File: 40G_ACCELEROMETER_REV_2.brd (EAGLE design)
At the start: 25.5 x 26.9 mm, 25 parts, among them IC1 3.3V_LDO, IC2 X_BUFFER, IC3 Y_BUFFER, IC4 Z_BUFFER

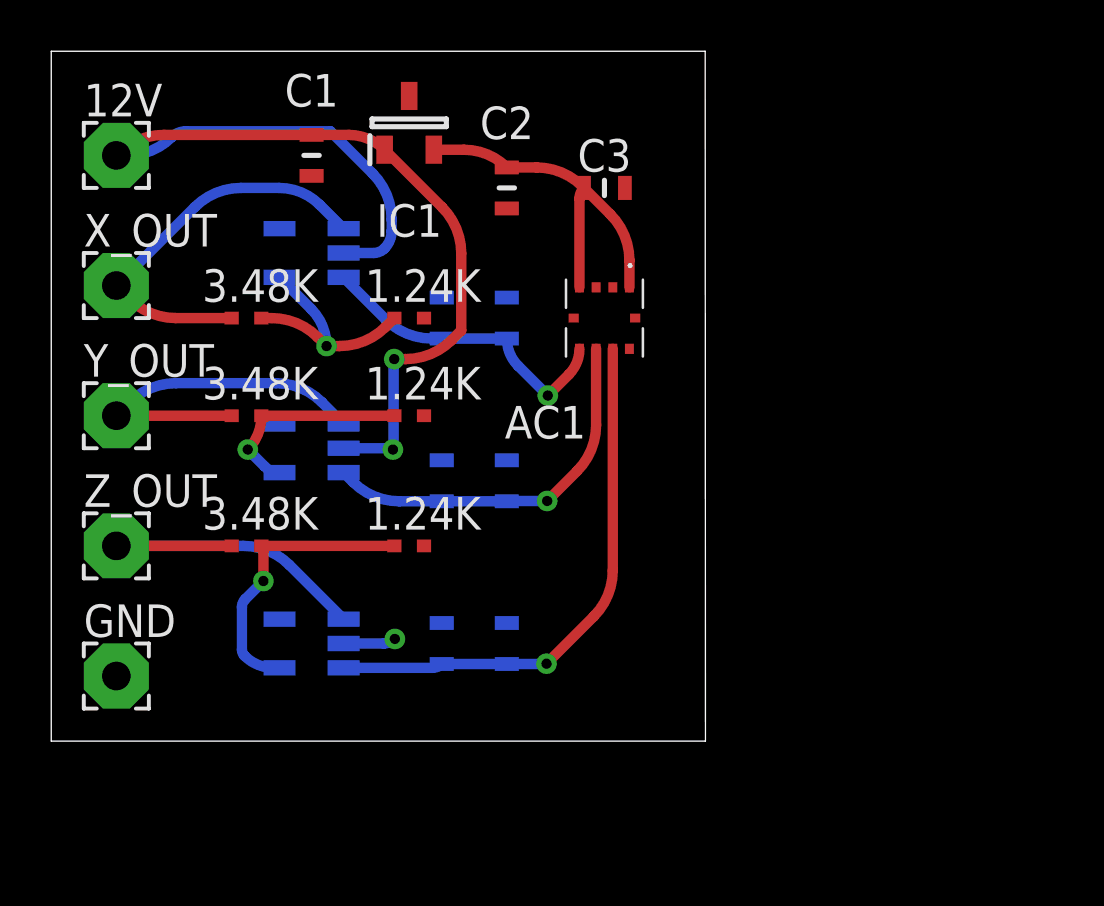
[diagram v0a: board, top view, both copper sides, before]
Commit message: Added ground plane to board
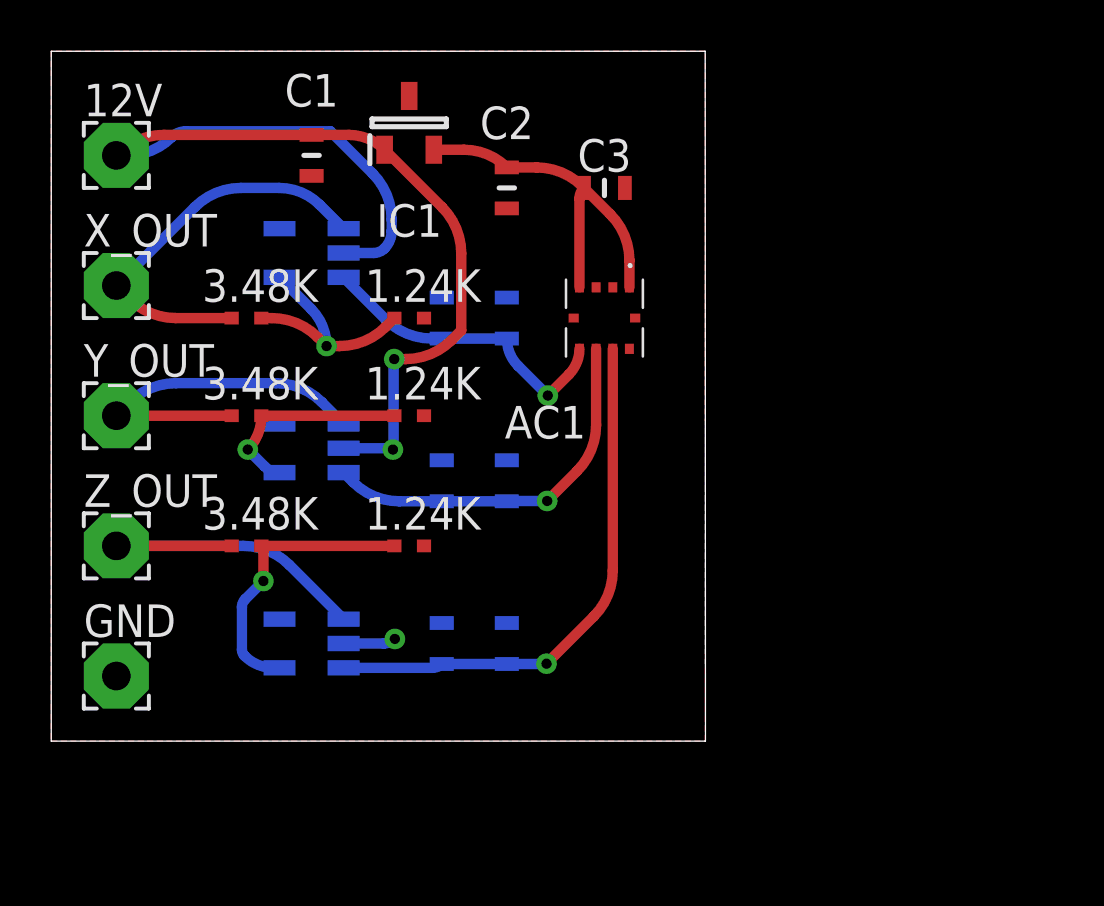
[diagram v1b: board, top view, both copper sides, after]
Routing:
- added copper zone on layer 1, net GND
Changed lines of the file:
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@@
 <setting verticaltext="up"/>
 </settings>
-<grid distance="1" unitdist="mil" unit="mil" style="lines" multiple="1" display="no" altdistance="1" altunitdist="mil" altunit="mil"/>
+<grid distance="10" unitdist="mil" unit="mil" style="lines" multiple="1" display="no" altdistance="5" altunitdist="mil" altunit="mil"/>
 <layers>
 <layer number="1" name="Top" color="4" fill="1" visible="yes" active="yes"/>
@@
 <layer number="14" name="Route14" color="22" fill="1" visible="no" active="no"/>
 <layer number="15" name="Route15" color="23" fill="1" visible="no" active="no"/>
-<layer number="16" name="Bottom" color="1" fill="1" visible="no" active="yes"/>
+<layer number="16" name="Bottom" color="1" fill="1" visible="yes" active="yes"/>
 <layer number="17" name="Pads" color="2" fill="1" visible="yes" active="yes"/>
 <layer number="18" name="Vias" color="2" fill="1" visible="yes" active="yes"/>
@@
 <layer number="20" name="Dimension" color="24" fill="1" visible="yes" active="yes"/>
 <layer number="21" name="tPlace" color="7" fill="1" visible="yes" active="yes"/>
-<layer number="22" name="bPlace" color="7" fill="1" visible="no" active="yes"/>
+<layer number="22" name="bPlace" color="7" fill="1" visible="yes" active="yes"/>
 <layer number="23" name="tOrigins" color="15" fill="1" visible="yes" active="yes"/>
-<layer number="24" name="bOrigins" color="15" fill="1" visible="no" active="yes"/>
+<layer number="24" name="bOrigins" color="15" fill="1" visible="yes" active="yes"/>
 <layer number="25" name="tNames" color="7" fill="1" visible="yes" active="yes"/>
-<layer number="26" name="bNames" color="7" fill="1" visible="no" active="yes"/>
+<layer number="26" name="bNames" color="7" fill="1" visible="yes" active="yes"/>
 <layer number="27" name="tValues" color="7" fill="1" visible="no" active="yes"/>
 <layer number="28" name="bValues" color="7" fill="1" visible="no" active="yes"/>
@@
 <layer number="38" name="bTest" color="7" fill="1" visible="no" active="yes"/>
 <layer number="39" name="tKeepout" color="4" fill="11" visible="yes" active="yes"/>
-<layer number="40" name="bKeepout" color="1" fill="11" visible="no" active="yes"/>
+<layer number="40" name="bKeepout" color="1" fill="11" visible="yes" active="yes"/>
 <layer number="41" name="tRestrict" color="4" fill="10" visible="yes" active="yes"/>
-<layer number="42" name="bRestrict" color="1" fill="10" visible="no" active="yes"/>
+<layer number="42" name="bRestrict" color="1" fill="10" visible="yes" active="yes"/>
 <layer number="43" name="vRestrict" color="2" fill="10" visible="no" active="yes"/>
 <layer number="44" name="Drills" color="7" fill="1" visible="no" active="yes"/>
@@
 <layer number="49" name="Reference" color="7" fill="1" visible="no" active="yes"/>
 <layer number="51" name="tDocu" color="7" fill="1" visible="yes" active="yes"/>
-<layer number="52" name="bDocu" color="7" fill="1" visible="no" active="yes"/>
+<layer number="52" name="bDocu" color="7" fill="1" visible="yes" active="yes"/>
 <layer number="88" name="SimResults" color="9" fill="1" visible="no" active="no"/>
 <layer number="89" name="SimProbes" color="9" fill="1" visible="no" active="no"/>
@@
 <contactref element="C3" pad="2"/>
 <contactref element="GND" pad="1"/>
-<wire x1="17.78" y1="10.96" x2="17.78" y2="17.31" width="0" layer="19" extent="16-16"/>
-<wire x1="17.78" y1="4.61" x2="17.78" y2="10.96" width="0" layer="19" extent="16-16"/>
-<wire x1="13.97" y1="25.18" x2="17.78" y2="17.31" width="0" layer="19" extent="1-16"/>
+<polygon width="0.254" layer="1" isolate="0.4064">
+<vertex x="0" y="0"/>
+<vertex x="25.527" y="0"/>
+<vertex x="25.527" y="26.924"/>
+<vertex x="0" y="26.924"/>
+</polygon>
+<wire x1="15.24" y1="17.31" x2="17.78" y2="17.31" width="0" layer="19" extent="16-16"/>
+<wire x1="14.5478" y1="16.51" x2="15.24" y2="17.31" width="0" layer="19" extent="1-16"/>
+<wire x1="17.78" y1="20.79" x2="17.78" y2="17.31" width="0" layer="19" extent="1-16"/>
+<wire x1="21.915" y1="17.71" x2="22.565" y2="15.31" width="0" layer="19" extent="1-1"/>
+<wire x1="14.5478" y1="12.7" x2="14.5478" y2="16.51" width="0" layer="19" extent="1-1"/>
+<wire x1="15.24" y1="10.96" x2="14.5478" y2="12.7" width="0" layer="19" extent="1-16"/>
+<wire x1="17.78" y1="10.96" x2="15.24" y2="10.96" width="0" layer="19" extent="16-16"/>
+<wire x1="14.5478" y1="7.62" x2="15.24" y2="10.96" width="0" layer="19" extent="1-16"/>
+<wire x1="15.24" y1="4.61" x2="14.5478" y2="7.62" width="0" layer="19" extent="1-16"/>
+<wire x1="17.78" y1="4.61" x2="15.24" y2="4.61" width="0" layer="19" extent="16-16"/>
 <wire x1="10.16" y1="22.06" x2="13.97" y2="25.18" width="0" layer="19" extent="1-1"/>
-<wire x1="17.78" y1="20.79" x2="13.97" y2="25.18" width="0" layer="19" extent="1-1"/>
-<wire x1="22.39" y1="21.59" x2="17.78" y2="20.79" width="0" layer="19" extent="1-1"/>
-<wire x1="21.265" y1="17.71" x2="22.39" y2="21.59" width="0" layer="19" extent="1-1"/>
-<wire x1="21.915" y1="17.71" x2="21.265" y2="17.71" width="0" layer="19" extent="1-1"/>
-<wire x1="22.565" y1="15.31" x2="21.915" y2="17.71" width="0" layer="19" extent="1-1"/>
-<wire x1="14.5478" y1="7.62" x2="17.78" y2="20.79" width="0" layer="19" extent="1-1"/>
+<wire x1="8.91" y1="20" x2="10.16" y2="22.06" width="0" layer="19" extent="1-16"/>
+<wire x1="8.91" y1="12.38" x2="14.5478" y2="12.7" width="0" layer="19" extent="1-16"/>
 <wire x1="8.91" y1="4.76" x2="14.5478" y2="7.62" width="0" layer="19" extent="1-16"/>
-<wire x1="14.5478" y1="12.7" x2="14.5478" y2="7.62" width="0" layer="19" extent="1-1"/>
-<wire x1="8.91" y1="12.38" x2="14.5478" y2="12.7" width="0" layer="19" extent="1-16"/>
-<wire x1="14.5478" y1="16.51" x2="8.91" y2="12.38" width="0" layer="19" extent="1-16"/>
-<wire x1="8.91" y1="20" x2="14.5478" y2="16.51" width="0" layer="19" extent="1-16"/>
-<wire x1="2.54" y1="2.54" x2="8.91" y2="20" width="0" layer="19" extent="16-16"/>
-<wire x1="15.24" y1="17.31" x2="17.78" y2="4.61" width="0" layer="19" extent="16-16"/>
-<wire x1="15.24" y1="10.96" x2="15.24" y2="17.31" width="0" layer="19" extent="16-16"/>
-<wire x1="15.24" y1="4.61" x2="15.24" y2="10.96" width="0" layer="19" extent="16-16"/>
 </signal>
 <signal name="X_SIG">

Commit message: Trying to add a ground plane that actually connects to all of the ground points
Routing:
- net 12V: track 45.0 -> 46.5 mm, vias 3 -> 4
- net REG3.3V: track 14.5 -> 13.0 mm
- added copper zone on layer 16, net GND
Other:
- board size 25.5 x 26.9 mm -> 25.4 x 26.9 mm

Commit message: Changed board layout
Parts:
- moved C8 1.83 mm to (13.7, 9.14), turned to 180 degrees
- moved C7 1.83 mm to (14.2, 18.0), turned to 180 degrees
- moved C2 1.48 mm to (16.5, 22.4)
- moved C3 0.92 mm to (22.4, 21.1), turned to 90 degrees
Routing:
- net 12V: track 46.5 -> 54.8 mm
- net REG3.3V: track 13.0 -> 17.3 mm
- net Y_SIG: track 14.8 -> 15.7 mm
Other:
- board text added: "Baja SAE 40G Accelerometer Designed By Anthony Bandak"

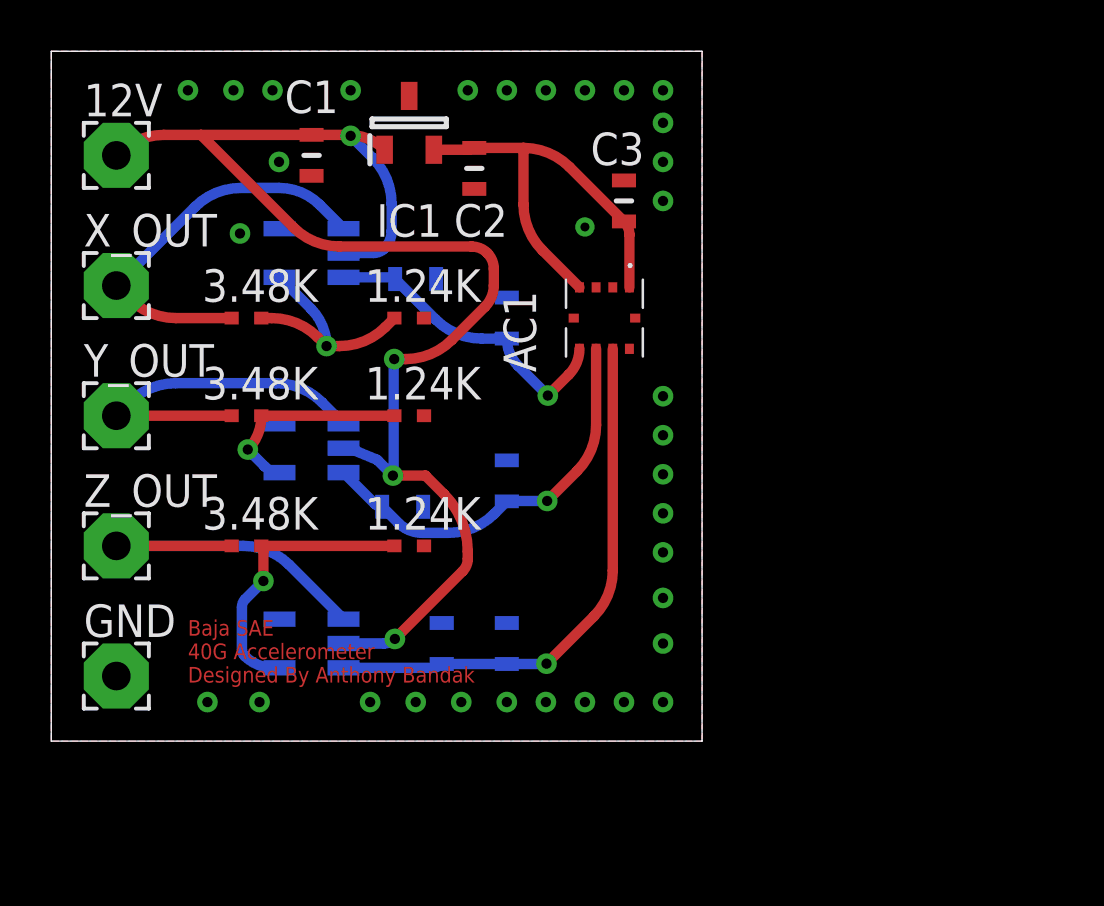
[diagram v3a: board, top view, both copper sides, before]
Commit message: New revision of board layout and fixed power connections to buffers in schematic.
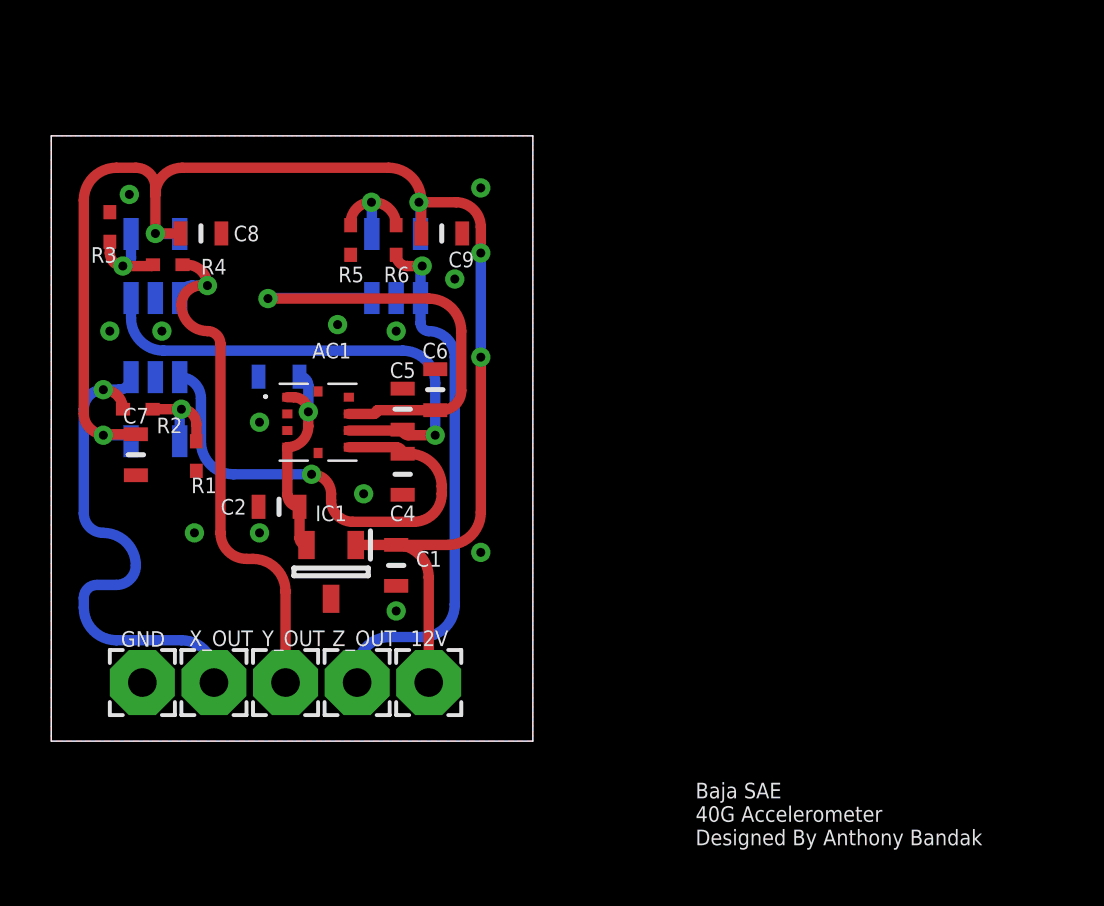
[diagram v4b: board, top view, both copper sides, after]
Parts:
- R1, R3, R5: value 1.24K -> TNPW04021K24BEED
- R2, R4, R6: value 3.48K -> TNPW04023K48BEED
- moved 12V 23.9 mm to (14.7, 2.29)
- moved IC1 17.8 mm to (10.9, 6.60), turned to 270 degrees
- moved C1 16.3 mm to (13.5, 6.86)
- moved C9 16.0 mm to (15.2, 19.8), flipped to the top, turned to 0 degrees
- moved X_OUT 16.0 mm to (6.35, 2.29)
- moved C2 15.2 mm to (8.89, 9.14), turned to 180 degrees
- moved C3 15.1 mm to (8.89, 14.2), flipped to the bottom, turned to 0 degrees
- moved IC4 15.1 mm to (13.5, 18.5), turned to 90 degrees
- moved R3 13.8 mm to (2.29, 20.1), turned to 90 degrees
- moved R6 13.3 mm to (13.5, 19.6), turned to 90 degrees
- moved C8 13.3 mm to (5.84, 19.8), flipped to the top, turned to 0 degrees
- moved C7 12.9 mm to (3.30, 11.2), flipped to the top, turned to 270 degrees
- moved Y_OUT 12.3 mm to (9.14, 2.29)
- moved R5 12.2 mm to (11.7, 19.6), turned to 270 degrees
- moved AC1 11.9 mm to (10.4, 12.4), turned to 0 degrees
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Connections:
- net 12V: now also C7.1, C8.1, C9.1, IC2.5, IC3.5, IC4.5; no longer IC2.2, IC3.2, IC4.2
- net GND: now also IC2.2, IC3.2, IC4.2; no longer IC2.5, IC3.5, IC4.5
- net X_SIG: no longer C7.1
- net Y_SIG: no longer C8.1
- net Z_SIG: no longer C9.1
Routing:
- net REG3.3V: track 17.3 -> 8.42 mm, vias 0 -> 1
- net Z_F/B: track 11.3 -> 3.81 mm
- net X_SIG: track 12.2 -> 18.7 mm
- net Y_OUT: track 14.2 -> 20.5 mm, vias 0 -> 1
- net Z_OUT: track 14.4 -> 20.4 mm, vias 0 -> 1
- net X_F/B: track 9.09 -> 3.89 mm
- net Y_F/B: track 8.18 -> 3.74 mm
- net X_OUT: track 15.7 -> 19.8 mm, vias 0 -> 1
- net 12V: track 54.8 -> 58.6 mm, vias 4 -> 5
- net Y_SIG: track 15.7 -> 19.2 mm
- net Z_SIG: track 21.1 -> 19.3 mm
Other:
- board size 25.4 x 26.9 mm -> 18.8 x 23.6 mm

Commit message: New layout for PCB board. Added diodes to main board pins. Ground stitching vias added. Ready for final review.
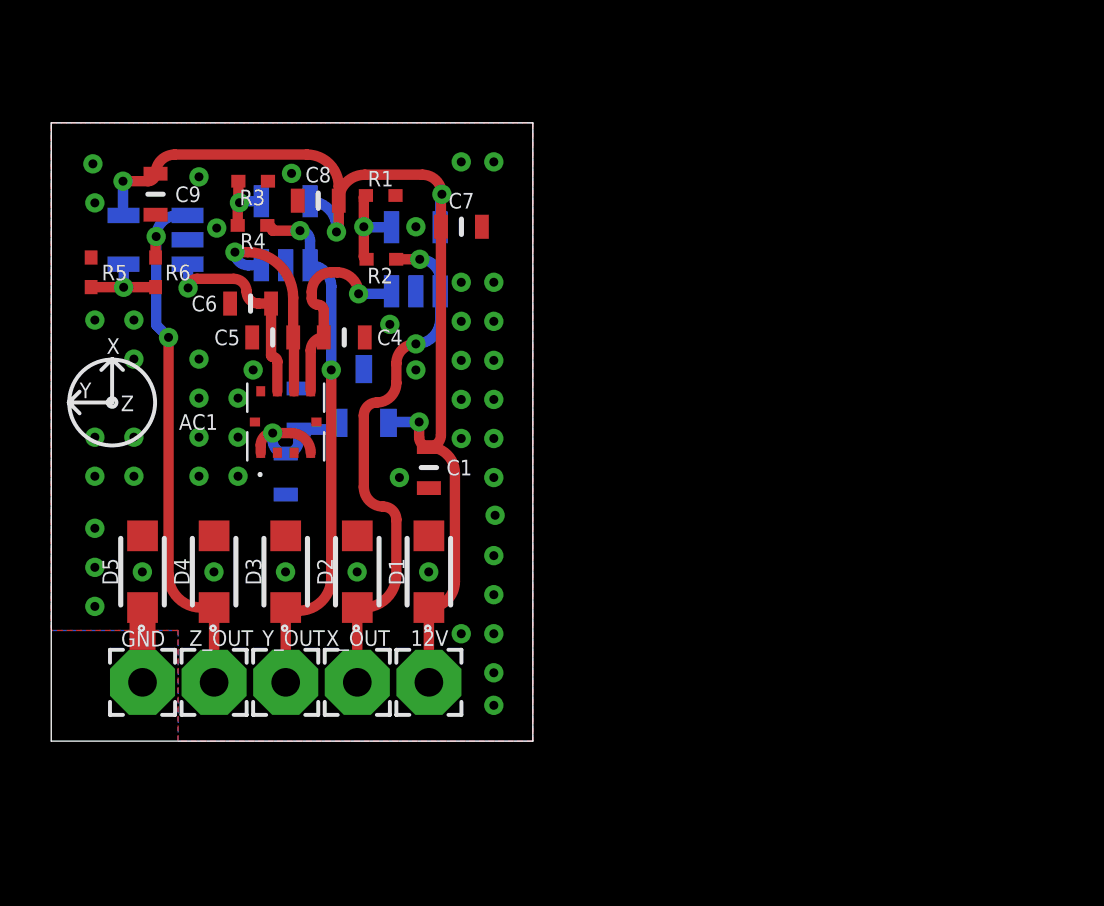
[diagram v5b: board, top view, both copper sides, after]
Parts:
- added D1, D2, D3, D4, D5: PTVS12VS1UR,115, SamacSys_Parts:SOD123W
- moved C7 15.5 mm to (16.0, 20.1), turned to 0 degrees
- moved R1 12.5 mm to (12.9, 21.3), turned to 0 degrees
- moved IC2 11.7 mm to (14.2, 18.8), turned to 90 degrees
- moved C9 11.3 mm to (4.07, 21.3), turned to 270 degrees
- moved R2 11.2 mm to (12.9, 18.8), turned to 180 degrees
- moved R5 10.2 mm to (1.56, 18.3), turned to 90 degrees
- moved R6 9.48 mm to (4.07, 18.3), turned to 270 degrees
- moved IC4 9.45 mm to (4.07, 19.6), turned to 0 degrees
- moved C6 7.95 mm to (7.78, 17.1), turned to 180 degrees
- moved IC1 6.98 mm to (12.2, 13.5), flipped to the bottom, turned to 90 degrees
- moved R3 5.87 mm to (7.88, 21.9), turned to 0 degrees
- moved C4 5.81 mm to (11.4, 15.8), turned to 0 degrees
- moved C5 5.80 mm to (8.64, 15.8), turned to 180 degrees
- moved X_OUT 5.59 mm to (11.9, 2.29)
- moved Z_OUT 5.58 mm to (6.36, 2.29)
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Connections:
- net 12V: now also D1.1
- net GND: now also D1.2, D2.2, D3.2, D4.2, D5.1, D5.2
- net X_OUT: now also D2.1
- net Y_OUT: now also D3.1
- net Z_OUT: now also D4.1
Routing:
- net 12V: track 58.6 -> 42.8 mm, vias 5 -> 4
- net Y_SIG: track 19.2 -> 7.92 mm
- net Z_SIG: track 19.3 -> 8.45 mm
- net X_SIG: track 18.7 -> 8.10 mm
- net GND: track 0.00 -> 2.92 mm, vias 13 -> 52
- net REG3.3V: track 8.42 -> 6.61 mm
- net Y_F/B: track 3.74 -> 2.65 mm
- net Z_OUT: track 20.4 -> 21.0 mm, vias 1 -> 2
- net X_OUT: track 19.8 -> 20.3 mm, vias 1 -> 2
- net Y_OUT: track 20.5 -> 20.7 mm, vias 1 -> 2
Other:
- board size 18.8 x 23.6 mm -> 18.8 x 24.1 mm
- board text added: "Baja SAE 2021-2022 40G Accelerometer Designed By Anthony Bandak"
- board text added: "X"
- board text added: "X-AXIS"
- board text added: "Y"
- board text added: "Y-AXIS"
- board text added: "Z"
- board text added: "Z-AXIS"
- board text removed: "Baja SAE 40G Accelerometer Designed By Anthony Bandak"
